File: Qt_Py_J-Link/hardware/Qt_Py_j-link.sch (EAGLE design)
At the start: 13 parts, among them U1 Qt Py SAMD21

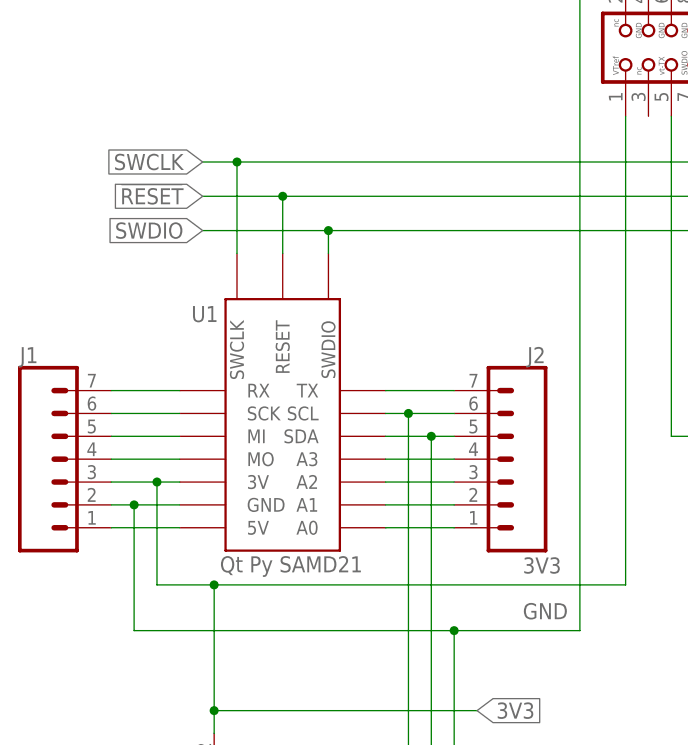
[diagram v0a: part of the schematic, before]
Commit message: reworked QT Py holes
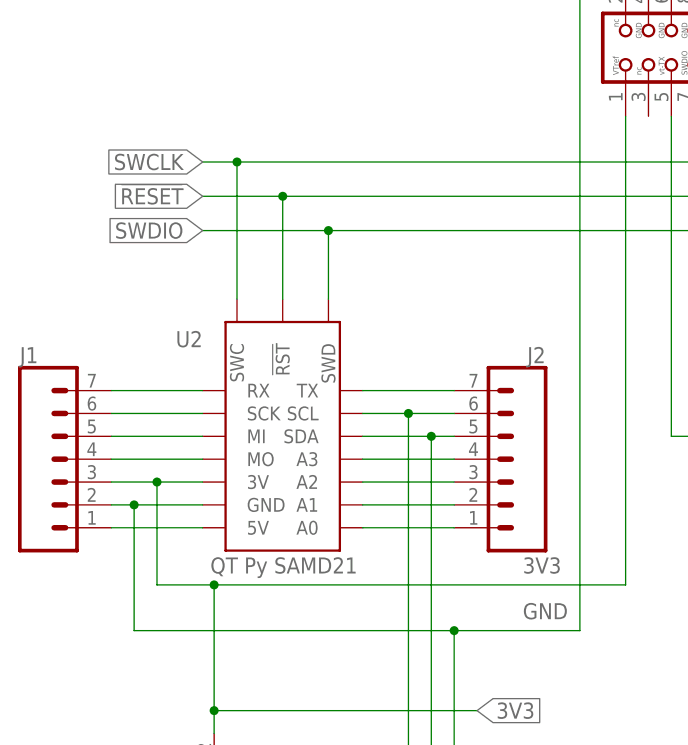
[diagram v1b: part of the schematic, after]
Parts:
- removed U1: Qt Py SAMD21, home:QT_PYTH
- added U2: QT Py SAMD21, home:QT_PY-SWD-TH
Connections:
- net !RESET: now also U2.!RST; no longer U1.RESET
- net 3V3: now also U2.3V; no longer U1.3V
- net 5V: now also U2.5V; no longer U1.5V
- net A0: now also U2.A0; no longer U1.A0
- net GND: now also U2.GND; no longer U1.GND
- net N$1: now also U2.RX; no longer U1.RX
- net N$14: now also U2.TX; no longer U1.TX
- net N$2: now also U2.SCK; no longer U1.SCK
- net N$3: now also U2.MI; no longer U1.MI
- net N$4: now also U2.MO; no longer U1.MO
- net N$5: now also U2.A3; no longer U1.A3
- net N$6: now also U2.A1; no longer U1.A1
- net N$8: now also U2.A2; no longer U1.A2
- net SCL: now also U2.SCL; no longer U1.SCL
- net SDA: now also U2.SDA; no longer U1.SDA
- net SWCLK: now also U2.SWC; no longer U1.SWCLK
- net SWDIO: now also U2.SWD; no longer U1.SWDIO
